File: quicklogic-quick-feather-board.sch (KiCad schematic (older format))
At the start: 35 parts, among them IC1 EOS-S3, J5 0473460001, U1 TPS62821DLCR, U2 MCP73831T-2ACI_OT, U3 GD25Q16CWIGR, X1 ECS-_327-12_5-34B-TR

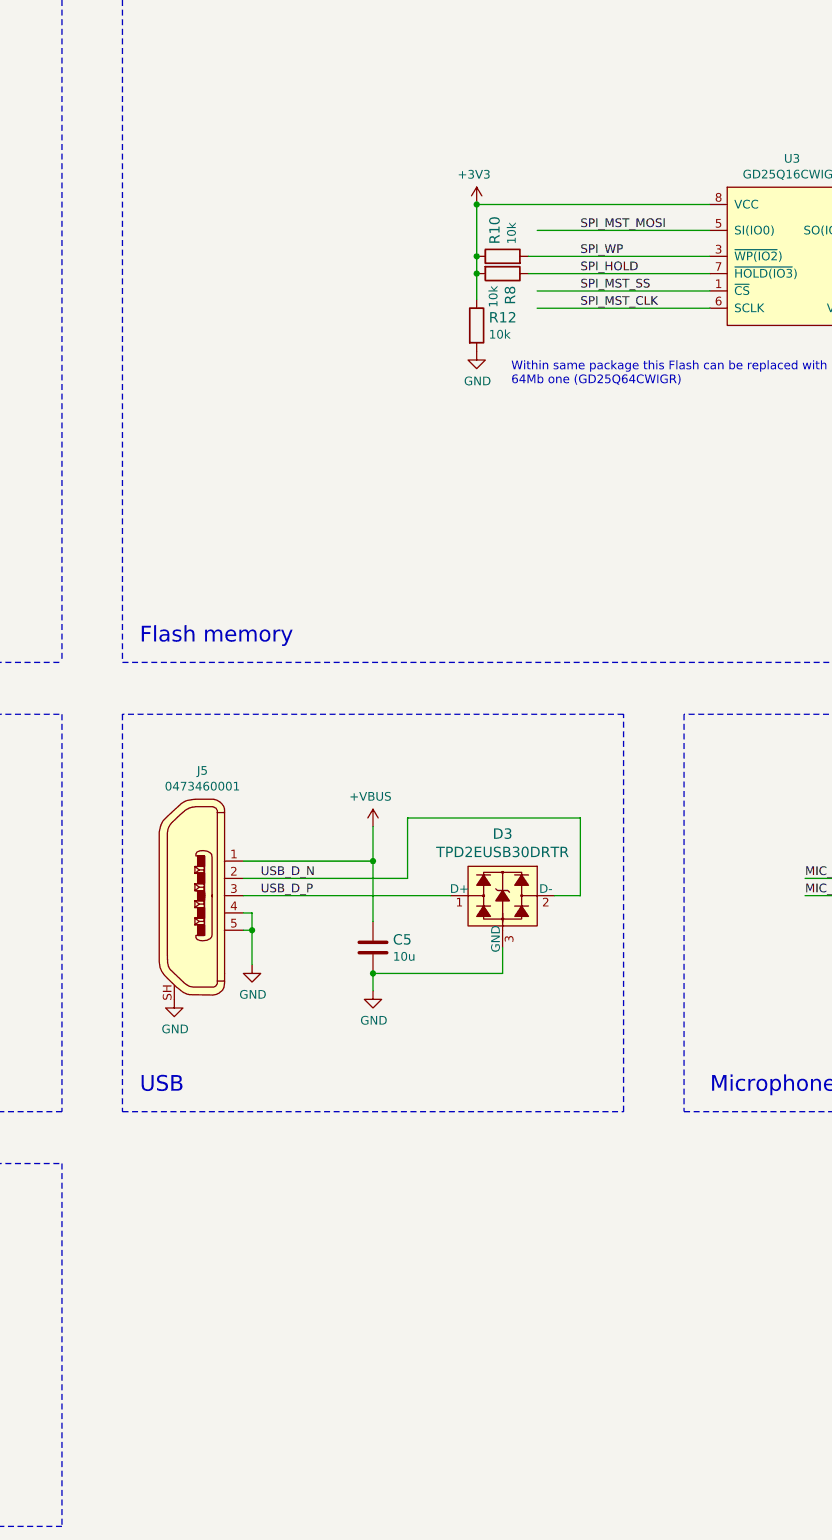
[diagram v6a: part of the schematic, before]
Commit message: Added pressure sensor
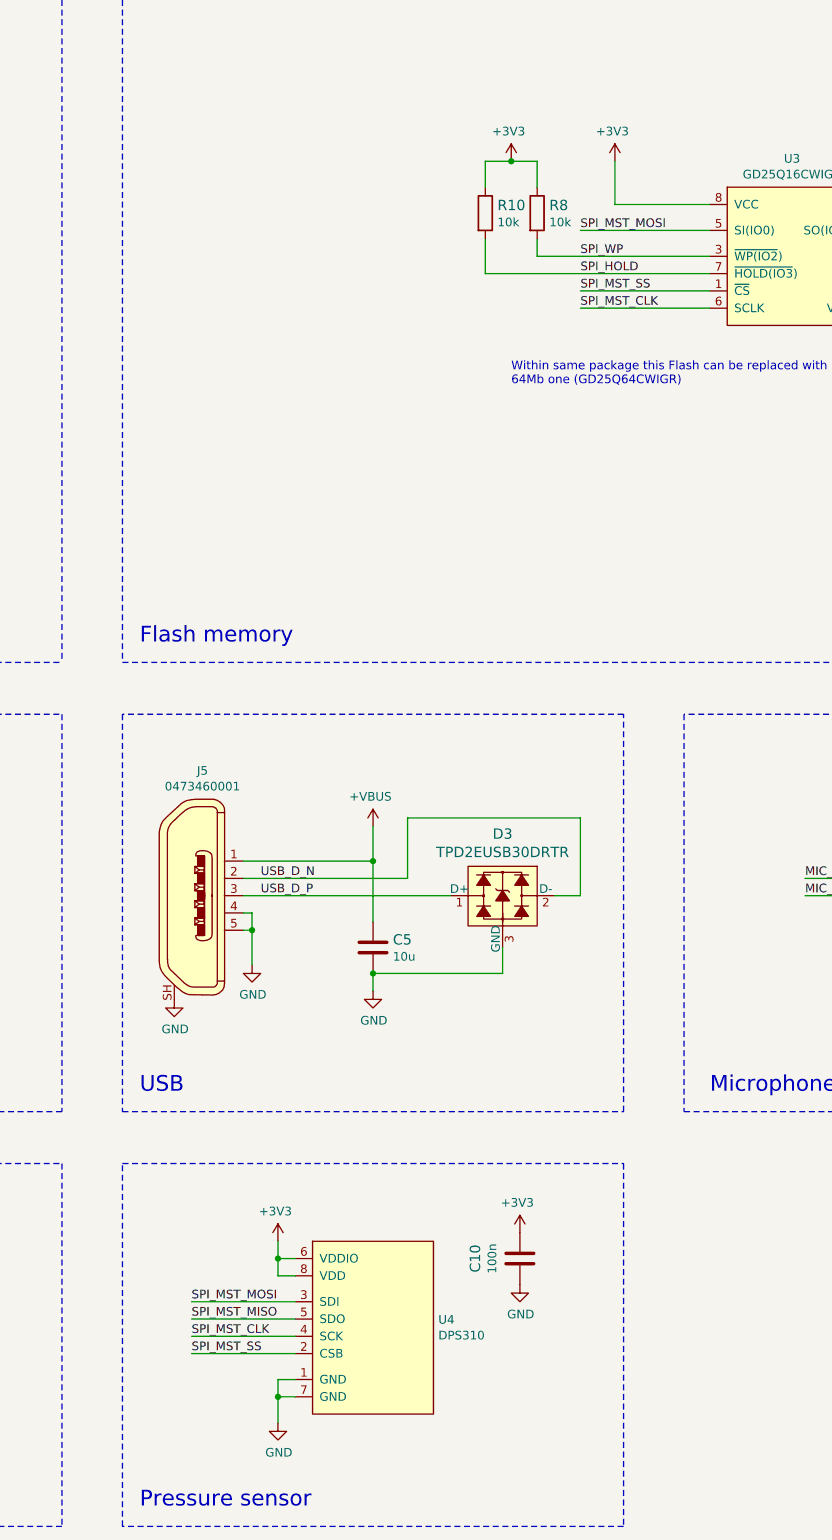
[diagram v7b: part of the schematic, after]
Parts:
- removed R12: R_10k_0402, quicklogic-quick-feather-board-footprints:0402-res, symbol quicklogic-quick-feather-board:R_10k_0402
- added C10: C_100n_0402_6V3, quicklogic-quick-feather-board-footprints:0402-cap, symbol quicklogic-quick-feather-board:C_100n_0402_6V3
- added U4: DPS310, antmicro-footprints:PG-VLGA-8-2, symbol antmicroSensorsTransducersAccessories:DPS310
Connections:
- wire segments 137 -> 153
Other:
- note added: "Pressure sensor"
- moved on the sheet: R10, R8
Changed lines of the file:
@@
 L quicklogic-quick-feather-board:R_10k_0402 R8
 U 1 1 5DC453B0
-P 10800 2950
-F 0 "R8" V 10755 3020 60  0000 L CNN
-F 1 "R_10k_0402" H 10800 2800 60  0001 C CNN
-F 2 "quicklogic-quick-feather-board-footprints:0402-res" H 11000 3150 60  0001 L CNN
-F 3 "" H 10800 2950 50  0001 C CNN
-F 4 "VISHAY" H 11000 3350 60  0001 L CNN "Manufacturer"
-F 5 "CRCW040210K0FKEDHP" H 11000 3250 60  0001 L CNN "MPN"
-F 6 "10k" V 10853 3020 50  0000 L CNN "Val"
-	1    10800 2950
-	-1   0    0    1
+P 11000 2600
+F 0 "R8" V 10955 2670 60  0000 L CNN
+F 1 "R_10k_0402" H 11000 2450 60  0001 C CNN
+F 2 "quicklogic-quick-feather-board-footprints:0402-res" H 11200 2800 60  0001 L CNN
+F 3 "" H 11000 2600 50  0001 C CNN
+F 4 "VISHAY" H 11200 3000 60  0001 L CNN "Manufacturer"
+F 5 "CRCW040210K0FKEDHP" H 11200 2900 60  0001 L CNN "MPN"
+F 6 "10k" V 11053 2670 50  0000 L CNN "Val"
+	1    11000 2600
+	0    1    1    0
 $EndComp
 $Comp
 L quicklogic-quick-feather-board:R_10k_0402 R10
 U 1 1 5DC484F8
-P 10800 2850
-F 0 "R10" V 10755 2920 60  0000 L CNN
-F 1 "R_10k_0402" H 10800 2700 60  0001 C CNN
-F 2 "quicklogic-quick-feather-board-footprints:0402-res" H 11000 3050 60  0001 L CNN
-F 3 "" H 10800 2850 50  0001 C CNN
-F 4 "VISHAY" H 11000 3250 60  0001 L CNN "Manufacturer"
-F 5 "CRCW040210K0FKEDHP" H 11000 3150 60  0001 L CNN "MPN"
-F 6 "10k" V 10853 2920 50  0000 L CNN "Val"
-	1    10800 2850
-	1    0    0    -1
+P 10700 2600
+F 0 "R10" V 10655 2670 60  0000 L CNN
+F 1 "R_10k_0402" H 10700 2450 60  0001 C CNN
+F 2 "quicklogic-quick-feather-board-footprints:0402-res" H 10900 2800 60  0001 L CNN
+F 3 "" H 10700 2600 50  0001 C CNN
+F 4 "VISHAY" H 10900 3000 60  0001 L CNN "Manufacturer"
+F 5 "CRCW040210K0FKEDHP" H 10900 2900 60  0001 L CNN "MPN"
+F 6 "10k" V 10753 2670 50  0000 L CNN "Val"
+	1    10700 2600
+	0    1    1    0
 $EndComp
 Wire Wire Line
 	12950 2700 13700 2700
 Wire Wire Line
-	11000 2700 12000 2700
-Wire Wire Line
-	11000 3150 12000 3150
-Wire Wire Line
-	11000 3050 12000 3050
+	11250 2700 12000 2700
+Wire Wire Line
+	11250 3150 12000 3150
+Wire Wire Line
+	11250 3050 12000 3050
 Text Notes 10850 3600 0    50   ~ 0
 Within same package this Flash can be replaced with \n64Mb one (GD25Q64CWIGR)
@@
 $EndBitmap
 Wire Wire Line
-	12000 2850 10950 2850
-Wire Wire Line
-	12000 2950 10950 2950
-Wire Wire Line
-	12000 2550 10650 2550
-Wire Wire Line
-	10650 2550 10650 2850
-Connection ~ 10650 2850
-Wire Wire Line
-	10650 2850 10650 2950
+	12000 2550 11450 2550
 $Comp
 L quicklogic-quick-feather-board:C_100n_0402_6V3 C8
@@
 	1    0    0    -1
 $EndComp
-Connection ~ 10650 2950
-$Comp
-L quicklogic-quick-feather-board:GND #PWR0110
-U 1 1 5DDB4DE8
-P 10650 3400
-F 0 "#PWR0110" H 10650 3150 50  0001 C CNN
-F 1 "GND" H 10655 3227 50  0000 C CNN
-F 2 "" H 10650 3400 50  0001 C CNN
-F 3 "" H 10650 3400 50  0001 C CNN
-	1    10650 3400
-	1    0    0    -1
-$EndComp
-Wire Wire Line
-	10650 2950 10650 3100
 $Comp
 L quicklogic-quick-feather-board:GND #PWR0111
@@
 	1    13200 3400
 	1    0    0    -1
-$EndComp
-$Comp
-L quicklogic-quick-feather-board:R_10k_0402 R12
-U 1 1 5DDC2D4F
-P 10650 3250
-F 0 "R12" V 10605 3320 60  0000 L CNN
-F 1 "R_10k_0402" H 10650 3100 60  0001 C CNN
-F 2 "quicklogic-quick-feather-board-footprints:0402-res" H 10850 3450 60  0001 L CNN
-F 3 "" H 10650 3250 50  0001 C CNN
-F 4 "VISHAY" H 10850 3650 60  0001 L CNN "Manufacturer"
-F 5 "CRCW040210K0FKEDHP" H 10850 3550 60  0001 L CNN "MPN"
-F 6 "10k" V 10703 3320 50  0000 L CNN "Val"
-	1    10650 3250
-	0    1    1    0
 $EndComp
 Text Label 11250 2850 0    50   ~ 0
@@
 L quicklogic-quick-feather-board:+3V3 #PWR0113
 U 1 1 5DE33E97
-P 10650 2500
-F 0 "#PWR0113" H 10650 2500 50  0001 C CNN
-F 1 "+3V3" H 10635 2623 50  0000 C CNN
-F 2 "" H 10650 2500 50  0001 C CNN
-F 3 "" H 10650 2500 50  0001 C CNN
-	1    10650 2500
-	1    0    0    -1
-$EndComp
-Connection ~ 10650 2550
+P 11450 2250
+F 0 "#PWR0113" H 11450 2250 50  0001 C CNN
+F 1 "+3V3" H 11435 2373 50  0000 C CNN
+F 2 "" H 11450 2250 50  0001 C CNN
+F 3 "" H 11450 2250 50  0001 C CNN
+	1    11450 2250
+	1    0    0    -1
+$EndComp
 $Comp
 L quicklogic-quick-feather-board:+3V3 #PWR0114
@@
 	10050 6150 10050 6350
 Connection ~ 10050 6350
+$Comp
+L antmicroSensorsTransducersAccessories:DPS310 U4
+U 1 1 5DDD6E59
+P 9700 8450
+F 0 "U4" H 10428 7896 50  0000 L CNN
+F 1 "DPS310" H 10428 7805 50  0000 L CNN
+F 2 "antmicro-footprints:PG-VLGA-8-2" H 9700 8500 50  0001 C CNN
+F 3 "https://www.infineon.com/dgdl/Infineon-DPS310-DataSheet-v01_01-EN.pdf?fileId=5546d462576f34750157750826c42242" H 9700 8450 50  0001 C CNN
+	1    9700 8450
+	1    0    0    -1
+$EndComp
+$Comp
+L quicklogic-quick-feather-board:+3V3 #PWR06
+U 1 1 5DDDD85D
+P 9500 8500
+F 0 "#PWR06" H 9500 8500 50  0001 C CNN
+F 1 "+3V3" H 9485 8623 50  0000 C CNN
+F 2 "" H 9500 8500 50  0001 C CNN
+F 3 "" H 9500 8500 50  0001 C CNN
+	1    9500 8500
+	1    0    0    -1
+$EndComp
+Wire Wire Line
+	9600 8650 9500 8650
+Wire Wire Line
+	9500 8650 9500 8550
+Wire Wire Line
+	9600 8750 9500 8750
+Wire Wire Line
+	9500 8750 9500 8650
+Connection ~ 9500 8650
+Wire Wire Line
+	9500 9350 9600 9350
+$Comp
+L quicklogic-quick-feather-board:GND #PWR07
+U 1 1 5DDEF120
+P 9500 9600
+F 0 "#PWR07" H 9500 9350 50  0001 C CNN
+F 1 "GND" H 9505 9427 50  0000 C CNN
+F 2 "" H 9500 9600 50  0001 C CNN
+F 3 "" H 9500 9600 50  0001 C CNN
+	1    9500 9600
+	1    0    0    -1
+$EndComp
+Wire Wire Line
+	9500 9350 9500 9450
+Wire Wire Line
+	9600 9450 9500 9450
+Connection ~ 9500 9450
+Wire Wire Line
+	9500 9450 9500 9600
+Text Label 9000 8900 0    50   ~ 0
+SPI_MST_MOSI
+Text Label 9000 9000 0    50   ~ 0
+SPI_MST_MISO
+Text Label 9000 9100 0    50   ~ 0
+SPI_MST_CLK
+Text Label 9000 9200 0    50   ~ 0
+SPI_MST_SS
+Wire Wire Line
+	9600 8900 9000 8900
+Wire Wire Line
+	9600 9000 9000 9000
+Wire Wire Line
+	9600 9100 9000 9100
+Wire Wire Line
+	9600 9200 9000 9200
+Wire Notes Line
+	8600 8100 11500 8100
+Wire Notes Line
+	11500 8100 11500 10200
+Wire Notes Line
+	11500 10200 8600 10200
+Wire Notes Line
+	8600 10200 8600 8100
+Text Notes 8700 10100 0    91   ~ 0
+Pressure sensor
+$Comp
+L quicklogic-quick-feather-board:C_100n_0402_6V3 C10
+U 1 1 5DE4CA75
+P 10900 8650
+F 0 "C10" V 10642 8650 60  0000 C CNN
+F 1 "C_100n_0402_6V3" H 10900 8500 60  0001 C CNN
+F 2 "quicklogic-quick-feather-board-footprints:0402-cap" H 11100 8850 60  0001 L CNN
+F 3 "" H 10900 8650 50  0001 C CNN
+F 4 "Walsin" H 11100 9050 60  0001 L CNN "Manufacturer"
+F 5 "0402X104K6R3CT" H 11100 8950 60  0001 L CNN "MPN"
+F 6 "100n" V 10740 8650 50  0000 C CNN "Val"
+	1    10900 8650
+	1    0    0    -1
+$EndComp
+$Comp
+L quicklogic-quick-feather-board:+3V3 #PWR08
+U 1 1 5DE5478B
+P 10900 8450
+F 0 "#PWR08" H 10900 8450 50  0001 C CNN
+F 1 "+3V3" H 10885 8573 50  0000 C CNN
+F 2 "" H 10900 8450 50  0001 C CNN
+F 3 "" H 10900 8450 50  0001 C CNN
+	1    10900 8450
+	1    0    0    -1
+$EndComp
+$Comp
+L quicklogic-quick-feather-board:GND #PWR09
+U 1 1 5DE54D9B
+P 10900 8800
+F 0 "#PWR09" H 10900 8550 50  0001 C CNN
+F 1 "GND" H 10905 8627 50  0000 C CNN
+F 2 "" H 10900 8800 50  0001 C CNN
+F 3 "" H 10900 8800 50  0001 C CNN
+	1    10900 8800
+	1    0    0    -1
+$EndComp
+$Comp
+L quicklogic-quick-feather-board:+3V3 #PWR?
+U 1 1 5DE86C59
+P 10850 2250
+F 0 "#PWR?" H 10850 2250 50  0001 C CNN
+F 1 "+3V3" H 10835 2373 50  0000 C CNN
+F 2 "" H 10850 2250 50  0001 C CNN
+F 3 "" H 10850 2250 50  0001 C CNN
+	1    10850 2250
+	1    0    0    -1
+$EndComp
+Wire Wire Line
+	11000 2450 11000 2300
+Wire Wire Line
+	11000 2300 10850 2300
+Wire Wire Line
+	10700 2450 10700 2300
+Wire Wire Line
+	10700 2300 10850 2300
+Connection ~ 10850 2300
+Wire Wire Line
+	11000 2850 11000 2750
+Wire Wire Line
+	11000 2850 12000 2850
+Wire Wire Line
+	10700 2950 10700 2750
+Wire Wire Line
+	10700 2950 12000 2950
+Wire Wire Line
+	11450 2300 11450 2550
 $EndSCHEMATC

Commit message: Added accelerometer and circuit for measuring battery voltage
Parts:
- removed U4: DPS310, antmicro-footprints:PG-VLGA-8-2, symbol antmicroSensorsTransducersAccessories:DPS310
- added C11: C_100n_0402_6V3, quicklogic-quick-feather-board-footprints:0402-cap, symbol quicklogic-quick-feather-board:C_100n_0402_6V3
- added Q1: BSS138AKA, quicklogic-quick-feather-board-footprints:SOT-23-3, symbol quicklogic-quick-feather-board:BSS138AKA
- added Q2: BSS84, quicklogic-quick-feather-board-footprints:SOT-23-3, symbol quicklogic-quick-feather-board:BSS84
- added R12, R17: R_100k_1%_0402, quicklogic-quick-feather-board-footprints:0402-res, symbol quicklogic-quick-feather-board:R_100k_1%_0402
- added R14, R15, R18, R19, R20: R_10k_0402, quicklogic-quick-feather-board-footprints:0402-res, symbol quicklogic-quick-feather-board:R_10k_0402
- added R16: R_200k_0402, quicklogic-quick-feather-board-footprints:0402-res, symbol quicklogic-quick-feather-board:R_200k_0402
- added U4: DPS310, quicklogic-quick-feather-board-footprints:PG-VLGA-8-2, symbol quicklogic-quick-feather-board:DPS310
- added U5: MC3635, quicklogic-quick-feather-board-footprints:MC3635, symbol quicklogic-quick-feather-board:MC3635
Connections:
- net labels added: ADC0, ADC0_EN, I2C_SCL, I2C_SDA, IMU_INT
- net labels removed: INT, IO31
- wire segments 153 -> 196
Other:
- note added: "Battery charger and battery voltage measurement"
- note added: "FBIO_8 and FBIO_9 are bootstrap pins for HS oscillator.\nThey should be pulled-down for internal HSO"
- note added: "IMU"
- note removed: "Battery charger"
- moved on the sheet: C2, C9, D2, R2, R3, U2
